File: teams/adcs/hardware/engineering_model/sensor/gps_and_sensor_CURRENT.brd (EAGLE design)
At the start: 90 x 90 mm, 50 parts, among them U1 TPS732XX, U2 TPS732XX, U3 OEM719, U4 LTC3624

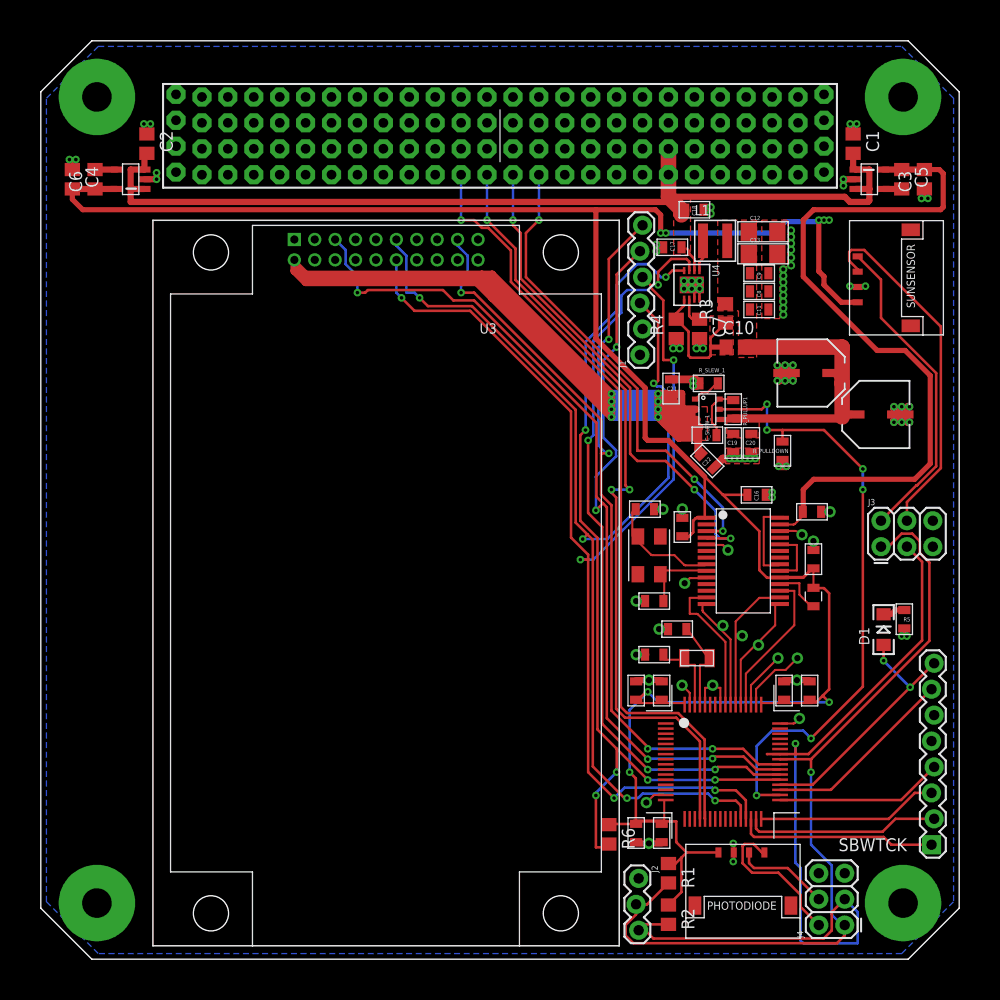
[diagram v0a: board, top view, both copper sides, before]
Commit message: ADCS/GPS: Rename to standardized part value naming scheme
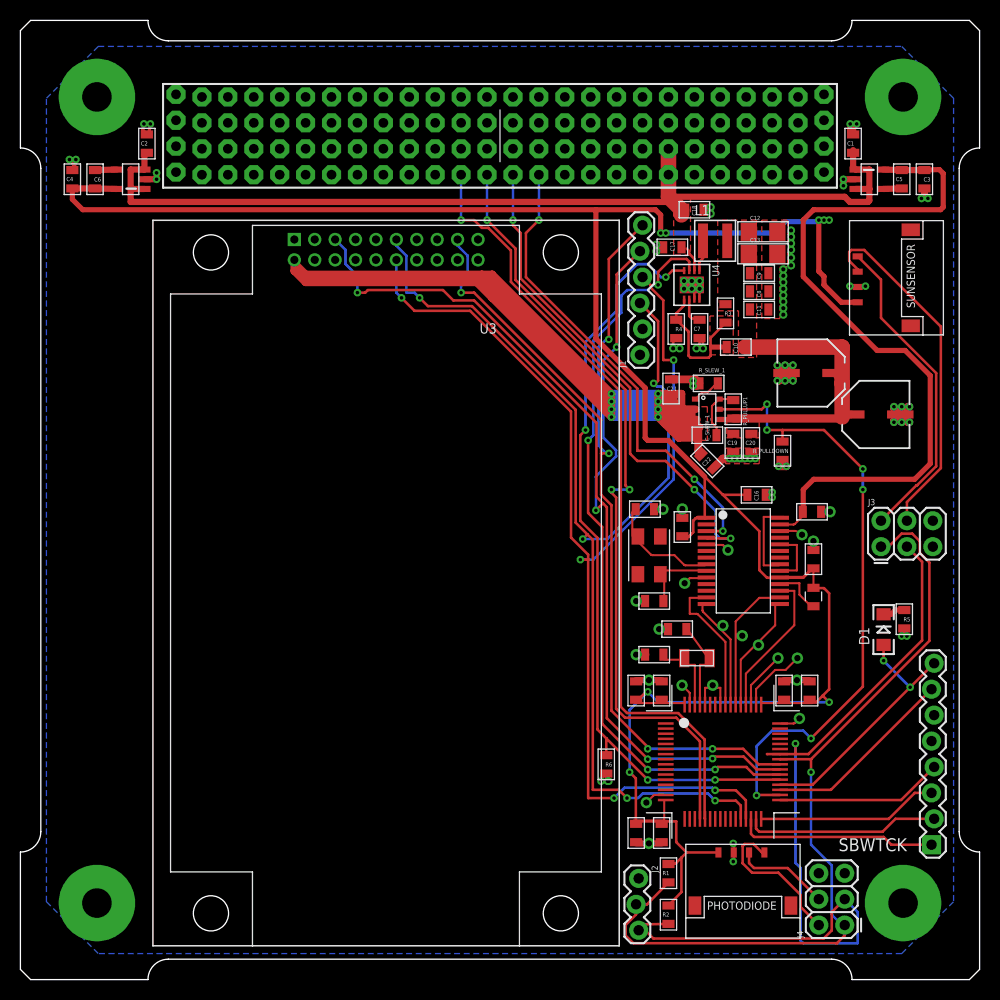
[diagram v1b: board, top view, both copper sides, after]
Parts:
- B1: value BOARD_TEMPLATE1 -> BOARD_TEMPLATESERCURED; device DubSat1 Components:BOARD_TEMPLATE -> DubSat1 Components:BOARD_TEMPLATE_SECURED
- C1, C2: value 1 μF -> 1u; device rcl:C0805 -> DubSat1 Components:0805
- C10: value 22pF -> 22p; device rcl:C0805 -> DubSat1 Components:0805
- C11, C17, C19, C21: value 10 uF -> 10u
- C12: value 47 uF -> 47u
- C13: value 22 uF -> 22u
- C14, C15: value 230 uF -> 230u
- C18, C20, C22, C9: value 1 uF -> 1u
- C3, C4: value 4.7 μF -> 4.7u; device rcl:C0805 -> DubSat1 Components:0805
- C5, C6: value 0.01 μF -> 0.01u; device rcl:C0805 -> DubSat1 Components:0805
- C7: value 2.2μF -> 2.2u; device rcl:C0805 -> DubSat1 Components:0805
- C8, C_SLEW_1: value 0.1 uF -> 0.1u
- R1, R2: value 2.2KΩ -> 2.2k; device rcl:R0805 -> DubSat1 Components:0805
- R3: value 450kΩ -> 100k; device rcl:R0805 -> DubSat1 Components:0805
- R4, R6: value 100kΩ -> 100k; device rcl:R0805 -> DubSat1 Components:0805
- R_SLEW_1: value 5k -> 1k
- U1, U2: value TPS732XX -> LT1761-X
- moved R6 6.86 mm to (61.2, 23.6), turned to 90 degrees
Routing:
- net 3V3_BUCK_PGOOD: track 86.4 -> 75.7 mm, vias 6 -> 4
- net N$10: track 2.54 -> 0.00 mm
- net +3V3: track 0.00 -> 1.82 mm, vias 0 -> 2
- net GPS_RXD1: track 115.3 -> 116.8 mm
- net GPS_TXD1: track 110.9 -> 112.2 mm
- net GND: track 53.1 -> 53.6 mm, vias 70 -> 71
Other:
- board size 90 x 90 mm -> 94 x 94 mm

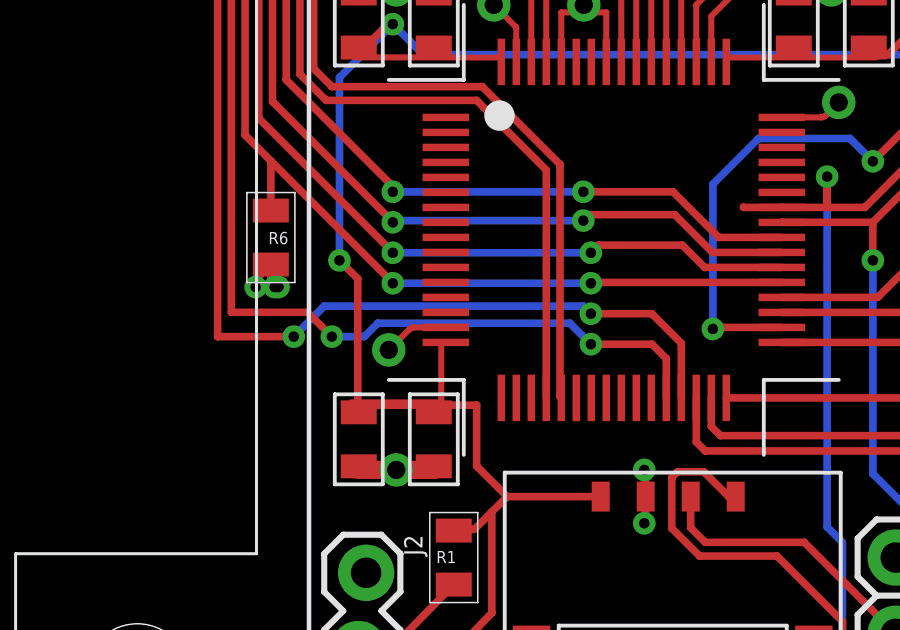
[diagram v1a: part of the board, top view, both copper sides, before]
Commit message: ADCS/GPS: TX/RX flip
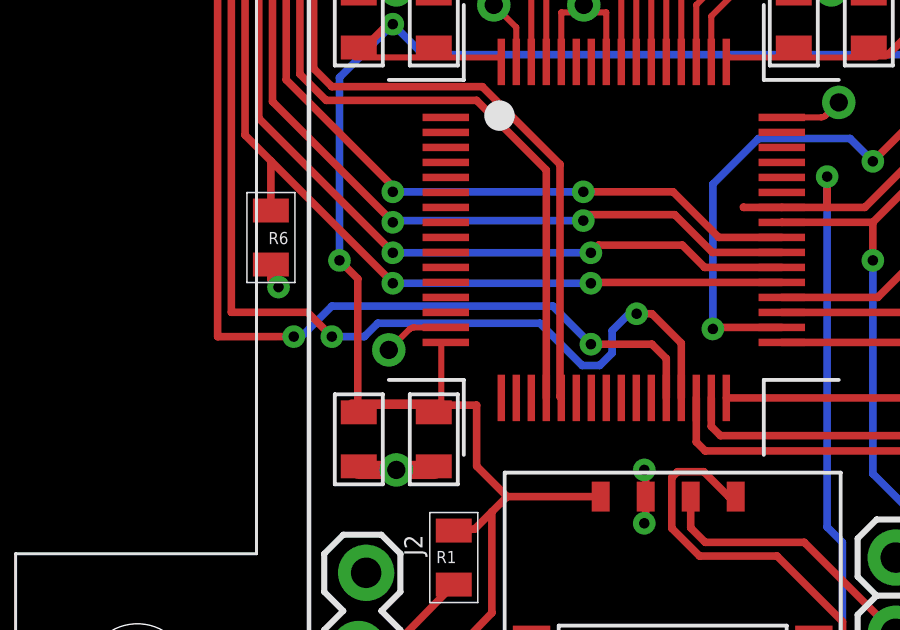
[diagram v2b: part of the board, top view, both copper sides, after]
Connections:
- net GPS_RXD1: now also BLK1.P2.5_GPIO; no longer BLK1.P2.6_GPIO/PWM
- net GPS_TXD1: now also BLK1.P2.6_GPIO/PWM; no longer BLK1.P2.5_GPIO
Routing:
- net GPS_TXD1: track 112.2 -> 114.9 mm
- net +3V3: track 1.82 -> 0.86 mm, vias 2 -> 1
- net GPS_RXD1: track 116.8 -> 116.0 mm
- net GND: vias 71 -> 70
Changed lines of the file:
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@@
 <?xml version="1.0" encoding="utf-8"?>
 <!DOCTYPE eagle SYSTEM "eagle.dtd">
-<eagle version="8.6.1">
+<eagle version="8.6.2">
 <drawing>
 <settings>
@@
 <wire x1="78.867" y1="52.832" x2="78.486" y2="53.213" width="0.762" layer="1"/>
 <wire x1="78.486" y1="53.213" x2="78.486" y2="53.456" width="0.762" layer="1"/>
-<via x="61.341" y="21.971" extent="1-16" drill="0.35" shape="square"/>
-<wire x1="65.144" y1="19.876" x2="61.341" y2="21.971" width="0" layer="19" extent="1-1"/>
 </signal>
 <signal name="VBAT">
@@
 <signal name="GPS_RXD1">
 <contactref element="U3" pad="P$12"/>
-<contactref element="BLK1" pad="P2.6_GPIO/PWM"/>
-<wire x1="71.882" y1="21.082" x2="73.914" y2="21.082" width="0.254" layer="1"/>
-<wire x1="74.894" y1="20.102" x2="73.914" y2="21.082" width="0.254" layer="1"/>
-<wire x1="74.894" y1="20.102" x2="74.894" y2="18.276" width="0.254" layer="1"/>
-<via x="71.882" y="21.082" extent="1-16" drill="0.35"/>
-<wire x1="71.882" y1="21.082" x2="71.628" y2="21.336" width="0.254" layer="16"/>
-<wire x1="62.992" y1="21.336" x2="61.976" y2="20.32" width="0.254" layer="16"/>
 <via x="61.976" y="20.32" extent="1-16" drill="0.35"/>
 <wire x1="61.976" y1="20.32" x2="59.4388" y2="20.3172" width="0.254" layer="1"/>
@@
 <wire x1="59.4388" y1="20.3172" x2="59.4388" y2="43.688" width="0.254" layer="1"/>
 <wire x1="59.4388" y1="43.688" x2="59.4388" y2="44.1700375" width="0.254" layer="1"/>
-<wire x1="71.628" y1="21.336" x2="62.992" y2="21.336" width="0.254" layer="16"/>
 <wire x1="57.7596" y1="58.17981875" x2="47.86741875" y2="68.072" width="0.254" layer="1"/>
 <contactref element="J1" pad="4"/>
@@
 <via x="41.148" y="69.342" extent="1-16" drill="0.35"/>
 <wire x1="41.148" y1="69.342" x2="40.64" y2="69.85" width="0.254" layer="16"/>
-</signal>
-<signal name="GPS_TXD1">
-<contactref element="U3" pad="P$11"/>
 <contactref element="BLK1" pad="P2.5_GPIO"/>
 <wire x1="74.394" y1="18.276" x2="74.394" y2="19.586" width="0.254" layer="1"/>
@@
 <wire x1="73.914" y1="20.066" x2="71.882" y2="20.066" width="0.254" layer="1"/>
 <via x="71.882" y="20.066" extent="1-16" drill="0.35"/>
-<wire x1="64.7757625" y1="20.765" x2="64.3307625" y2="20.32" width="0.254" layer="16"/>
-<wire x1="64.3307625" y1="20.32" x2="63.246" y2="20.32" width="0.254" layer="16"/>
-<wire x1="71.882" y1="20.066" x2="71.183" y2="20.765" width="0.254" layer="16"/>
-<wire x1="71.183" y1="20.765" x2="64.7757625" y2="20.765" width="0.254" layer="16"/>
+<wire x1="61.976" y1="20.32" x2="62.23" y2="20.32" width="0.254" layer="16"/>
+<wire x1="62.23" y1="20.32" x2="63.246" y2="21.336" width="0.254" layer="16"/>
+<wire x1="63.246" y1="21.336" x2="70.612" y2="21.336" width="0.254" layer="16"/>
+<wire x1="70.612" y1="21.336" x2="71.882" y2="20.066" width="0.254" layer="16"/>
+</signal>
+<signal name="GPS_TXD1">
+<contactref element="U3" pad="P$11"/>
 <wire x1="58.2168" y1="47.30861875" x2="59.366709375" y2="46.158709375" width="0.254" layer="1"/>
 <wire x1="59.366709375" y1="46.158709375" x2="59.896" y2="45.62941875" width="0.254" layer="1"/>
@@
 <wire x1="59.896" y1="21.13" x2="62.436" y2="21.13" width="0.254" layer="1"/>
 <wire x1="62.436" y1="21.13" x2="63.246" y2="20.32" width="0.254" layer="1"/>
+<contactref element="BLK1" pad="P2.6_GPIO/PWM"/>
+<wire x1="73.406" y1="21.082" x2="73.914" y2="21.082" width="0.254" layer="1"/>
+<wire x1="74.894" y1="20.102" x2="73.914" y2="21.082" width="0.254" layer="1"/>
+<wire x1="74.894" y1="20.102" x2="74.894" y2="18.276" width="0.254" layer="1"/>
+<via x="73.406" y="21.082" extent="1-16" drill="0.35"/>
+<wire x1="63.246" y1="20.32" x2="64.3307625" y2="20.32" width="0.254" layer="16"/>
+<wire x1="64.3307625" y1="20.32" x2="64.7757625" y2="20.765" width="0.254" layer="16"/>
+<wire x1="71.58856875" y1="19.3576" x2="72.17543125" y2="19.3576" width="0.254" layer="16"/>
+<wire x1="72.17543125" y1="19.3576" x2="72.5904" y2="19.77256875" width="0.254" layer="16"/>
+<wire x1="73.152" y1="21.082" x2="72.5904" y2="20.5204" width="0.254" layer="16"/>
+<wire x1="72.5904" y1="19.77256875" x2="72.5904" y2="20.5204" width="0.254" layer="16"/>
+<wire x1="64.7757625" y1="20.765" x2="70.18116875" y2="20.765" width="0.254" layer="16"/>
+<wire x1="70.18116875" y1="20.765" x2="71.58856875" y2="19.3576" width="0.254" layer="16"/>
+<wire x1="73.406" y1="21.082" x2="73.152" y2="21.082" width="0.254" layer="16"/>
 </signal>
 <signal name="N$1">
@@
 <signal name="+3V3">
 <contactref element="R6" pad="1"/>
-<via x="60.706" y="21.971" extent="1-16" drill="0.35" shape="square"/>
 <via x="61.468" y="21.971" extent="1-16" drill="0.35" shape="square"/>
-<wire x1="60.706" y1="21.971" x2="60.706" y2="22.214" width="0.254" layer="1"/>
-<wire x1="60.706" y1="22.214" x2="61.214" y2="22.722" width="0.254" layer="1"/>
 <wire x1="61.468" y1="21.971" x2="61.214" y2="22.225" width="0.254" layer="1"/>
 <wire x1="61.214" y1="22.225" x2="61.214" y2="22.722" width="0.254" layer="1"/>

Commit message: ADCS/GPS: Fix resistor values for buck converter
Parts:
- R3: value 100k -> 0
- R4: value 100k -> DNP
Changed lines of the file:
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@@
 <?xml version="1.0" encoding="utf-8"?>
 <!DOCTYPE eagle SYSTEM "eagle.dtd">
-<eagle version="8.6.2">
+<eagle version="8.6.3">
 <drawing>
 <settings>
@@
 <element name="C7" library="DubSat1 Components" package="0805" value="2.2u" x="70.358" y="66.294" rot="R270"/>
 <element name="L1" library="DubSat1 Components" package="COILCRAFT_XAL4020" value="COILCRAFT_XAL4020-222ME" x="71.882" y="74.93"/>
-<element name="R3" library="DubSat1 Components" package="0805" value="100k" x="72.898" y="67.818" rot="R90"/>
-<element name="R4" library="DubSat1 Components" package="0805" value="100k" x="68.072" y="66.294" rot="R90"/>
+<element name="R3" library="DubSat1 Components" package="0805" value="0" x="72.898" y="67.818" rot="R90"/>
+<element name="R4" library="DubSat1 Components" package="0805" value="DNP" x="68.072" y="66.294" rot="R90"/>
 <element name="C10" library="DubSat1 Components" package="0805" value="22p" x="73.914" y="64.516"/>
 <element name="C8" library="DubSat1 Components" package="0805" value="0.1u" x="76.2" y="69.977"/>
